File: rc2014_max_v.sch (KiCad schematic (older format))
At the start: 12 parts, among them IC1 SN74ALVC164245DGG, IC2 5M570ZT100I5N, IC3 SN74ALVC164245DGG, J1 Z80 Bus, J2 Pro Bus, J4 M3 Mounting Hole, U1 MIC5356-SGYMME, U2 SN74AVC8T245PW

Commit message: reorganized pins
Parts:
- removed IC1, IC3: SN74ALVC164245DGG, Package_SO:TSSOP-48_6.1x12.5mm_P0.5mm, symbol SN74ALVC164245DGG:SN74ALVC164245DGG
- removed IC2: 5M570ZT100I5N, QFP50P1600X1600X120-100N, symbol 5M570ZT100I5N:5M570ZT100I5N
- removed U2: SN74AVC8T245PW, Package_SO:TSSOP-24_4.4x7.8mm_P0.65mm, symbol Logic_LevelTranslator:SN74AVC8T245PW
- added C10, C11, C12, C13, C14, C15, C16, C5, C6, C7, C8, C9: 100nF, Capacitor_SMD:C_0805_2012Metric_Pad1.15x1.40mm_HandSolder, symbol Device:C
- added U2, U3, U5: SN74ALVC164245DGG, Package_SO:TSSOP-48_6.1x12.5mm_P0.5mm, symbol rc2014_max_v-rescue:SN74ALVC164245DGG
- added U4: 5M570ZT100I5N, Package_QFP:TQFP-100_14x14mm_P0.5mm, symbol rc2014_max_v-rescue:5M570ZT100I5N
- C1, C2, C3, C4: footprint Capacitor_THT:C_Disc_D3.8mm_W2.6mm_P2.50mm -> Capacitor_SMD:C_0805_2012Metric_Pad1.15x1.40mm_HandSolder
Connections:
- net labels added: ~DIR
- wire segments 46 -> 121
- no-connect marks 13 -> 8
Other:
- moved on the sheet: J4

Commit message: numerous changes
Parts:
- removed C13, C15: 100nF, Capacitor_SMD:C_0805_2012Metric_Pad1.15x1.40mm_HandSolder, symbol Device:C
- removed U2, U3, U5: SN74ALVC164245DGG, Package_SO:TSSOP-48_6.1x12.5mm_P0.5mm, symbol rc2014_max_v-rescue:SN74ALVC164245DGG
- C1, C10, C11, C12, C14, C16, C2, C3, C4, C5, C6, C7, C8, C9: footprint Capacitor_SMD:C_0805_2012Metric_Pad1.15x1.40mm_HandSolder -> Capacitor_SMD:C_0603_1608Metric_Pad1.05x0.95mm_HandSolder
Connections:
- net labels removed: DIR, ~DIR
- wire segments 121 -> 74
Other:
- moved on the sheet: C2, C3, C4, U4

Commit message: added FT JTAG
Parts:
- removed U4: 5M570ZT100I5N, Package_QFP:TQFP-100_14x14mm_P0.5mm, symbol rc2014_max_v-rescue:5M570ZT100I5N
- added C13, C15: 100nF, Capacitor_SMD:C_0603_1608Metric_Pad1.05x0.95mm_HandSolder, symbol Device:C
- added J8: Pro Bus, Connector_PinHeader_2.54mm:PinHeader_1x16_P2.54mm_Horizontal, symbol Connector_Generic:Conn_01x16
- added U10, U2, U3, U4: SN74ALVC164245DGG, Package_SO:TSSOP-48_6.1x12.5mm_P0.5mm, symbol rc2014_max_v-rescue:SN74ALVC164245DGG
- J1: value Z80 Bus -> Conn_01x39; footprint Connector_PinHeader_2.54mm:PinHeader_1x39_P2.54mm_Vertical -> Connector_PinHeader_2.54mm:PinHeader_1x39_P2.54mm_Horizontal; MFR - -> (none); MPN - -> (none); SPN - -> (none); SPR - -> (none); SPURL - -> (none)
- J2: value Pro Bus -> Conn_01x10
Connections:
- net labels added: A0_F, A10_F, A11_F, A12_F, A13_F, A14_F, A15_F, A1_F, A2_F, A3_F, A4_F, A5_F, A6_F, A7_F, A8_F, A9_F, CLK_F, D0_F, D1_F, D2_F, D3_F, D4_F, D5_F, D6_F, D7_F, DIR, GPIO_1, GPIO_10, GPIO_11, GPIO_12, GPIO_13, GPIO_14, GPIO_15, GPIO_16, GPIO_2, GPIO_3, GPIO_4, GPIO_5, GPIO_6, GPIO_7, GPIO_8, GPIO_9, OE_A, OE_C_I, OE_C_O, OE_D, RX_A, TX_A, ~BUSACK_F, ~DIR, ~IORQ_F, ~M1_F, ~MREQ_F, ~PAGE_F, ~RD_F, ~WR_F
- wire segments 74 -> 114
- no-connect marks 8 -> 5
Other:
- moved on the sheet: C1, C2, C3, C4, J4

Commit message: replaced single resistors with arrays
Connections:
- net labels added: RX_A_F, ~BUSRQ_F, ~HALT_F, ~INT_F, ~NMI_F, ~RESET2_F, ~RESET_F, ~WAIT_F
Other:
- moved on the sheet: C10, C11, C12, C13, C14, C15, C16, C2, C3, C4, C5, C6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

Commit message: fixed up GPIO, started layout
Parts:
- removed U10: SN74ALVC164245DGG, Package_SO:TSSOP-48_6.1x12.5mm_P0.5mm, symbol rc2014_max_v-rescue:SN74ALVC164245DGG
- added C16, C17: 100nF, Capacitor_SMD:C_0603_1608Metric_Pad1.05x0.95mm_HandSolder, symbol Device:C
- added R1, R2: 50K, Resistor_SMD:R_0603_1608Metric_Pad1.05x0.95mm_HandSolder, symbol Device:R_Small
- added U4, U5: TXB0108PWR, Package_SO:TSSOP-20_4.4x6.5mm_P0.65mm, symbol Logic_LevelTranslator:TXB0108PWR
- J2: renamed from J1; value Conn_01x39 -> Conn_01x40; footprint Connector_PinHeader_2.54mm:PinHeader_1x39_P2.54mm_Horizontal -> Connector_PinHeader_2.54mm:PinHeader_1x40_P2.54mm_Horizontal; symbol Connector_Generic:Conn_01x39 -> Connector_Generic:Conn_01x40
- J4: renamed from J2; value Conn_01x10 -> Conn_01x24; footprint Connector_PinHeader_2.54mm:PinHeader_1x10_P2.54mm_Vertical -> Connector_PinHeader_2.54mm:PinHeader_1x24_P2.54mm_Vertical; symbol Connector_Generic:Conn_01x10 -> Connector_Generic:Conn_01x24
- U1: symbol Regulator_Linear:MIC5356-SGYMME -> rc2014_max_v-rescue:MIC5356-SGYMME-Regulator_Linear
- renumbered C11 to C1, C5 to C10, C6 to C11, C7 to C12, C8 to C13, C9 to C14, C10 to C15, C1 to C18, C12 to C2, C13 to C3, C14 to C4, C15 to C5, C16 to C6, C3 to C7, C2 to C8, C4 to C9, J4 to J1, J8 to J3, U4 to U2, U2 to U6
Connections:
- net labels added: D10, D10_F, D11, D11_F, D12, D12_F, D13, D13_F, D14, D14_F, D15, D15_F, D8, D8_F, D9, D9_F, OE_G_1, OE_G_2, RX_B, TX_B
- wire segments 114 -> 113
- no-connect marks 5 -> 9
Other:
- moved on the sheet: C1, C10, C11, C12, C13, C14, C15, C2, C3, C4, C5, C6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

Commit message: Added logo, cpio vcc selection
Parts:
- added JP1: Jumper_3_Bridged12, Connector_PinHeader_2.54mm:PinHeader_1x03_P2.54mm_Vertical, symbol Jumper:Jumper_3_Bridged12
- U4, U5: symbol Logic_LevelTranslator:TXB0108PWR -> rc2014_max_v-rescue:TXB0108PWR-Logic_LevelTranslator
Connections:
- net +3V3: now also JP1.1 (A)
- net +5V: now also JP1.3 (B); no longer C16.1, C17.1, U4.19 (VCCB), U5.19 (VCCB)
- new net VCC_GPIO: C16.1, C17.1, JP1.2 (C), U4.19 (VCCB), U5.19 (VCCB)
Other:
- moved on the sheet: C16, C17, R2, U5

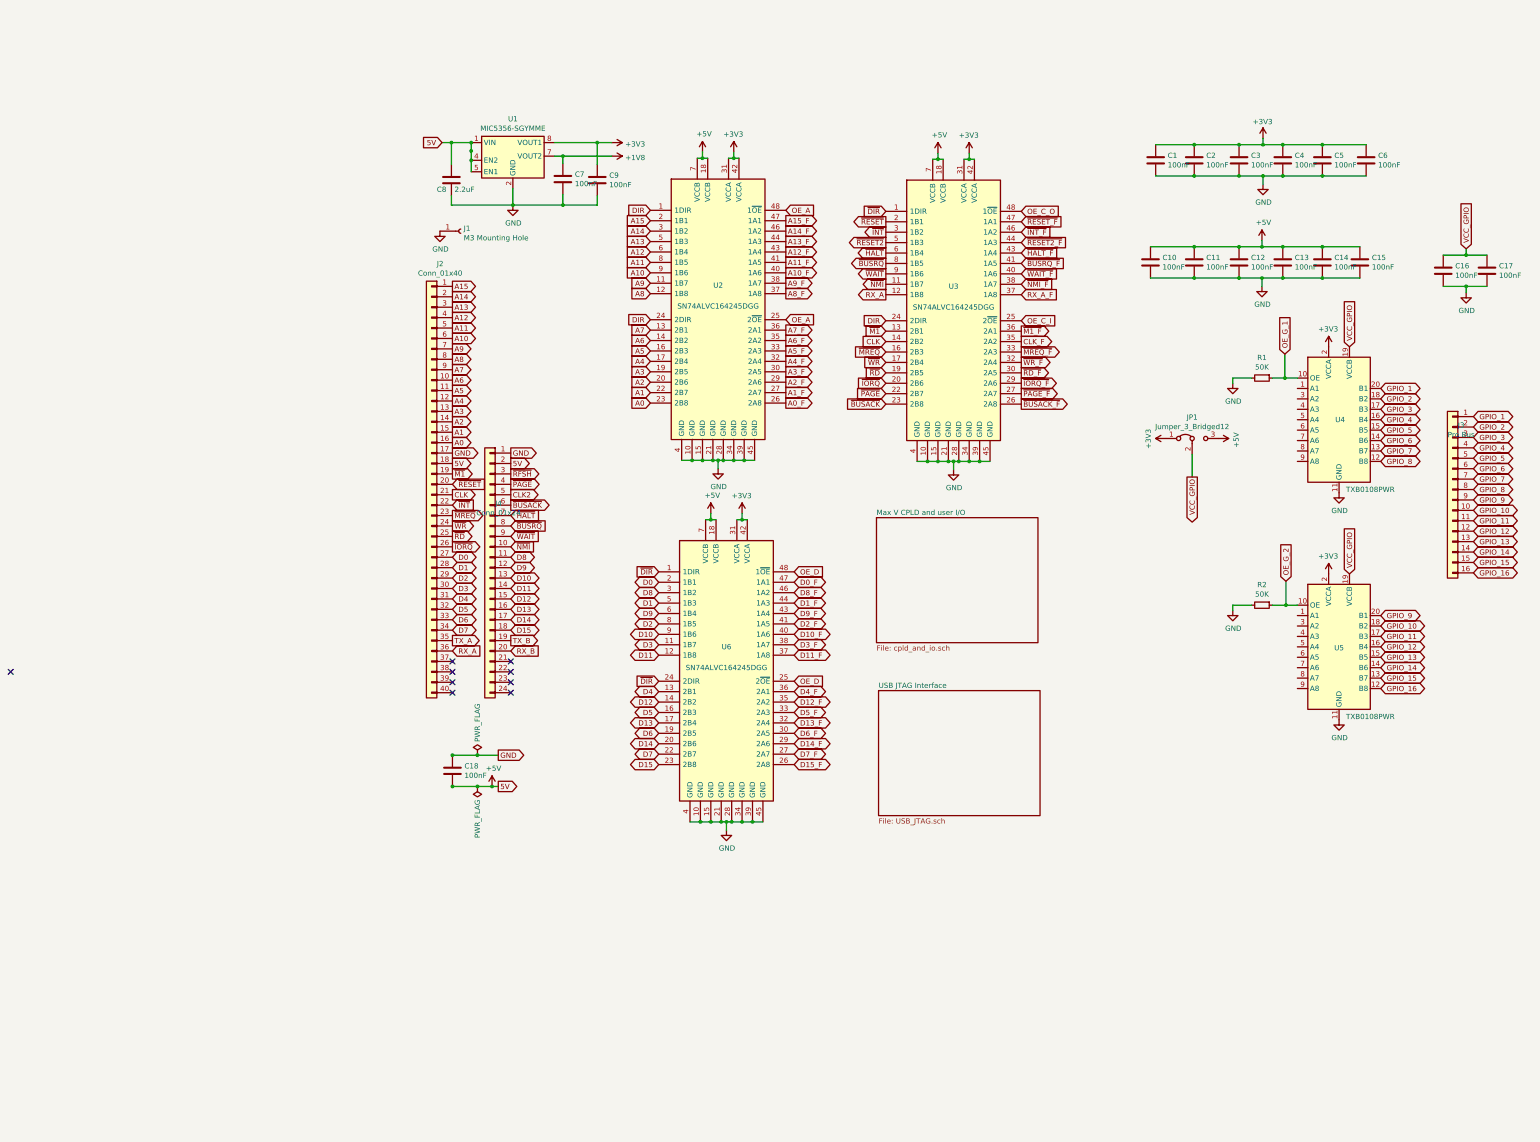
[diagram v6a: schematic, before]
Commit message: larger maxv, additional clocks, reorganized sheets
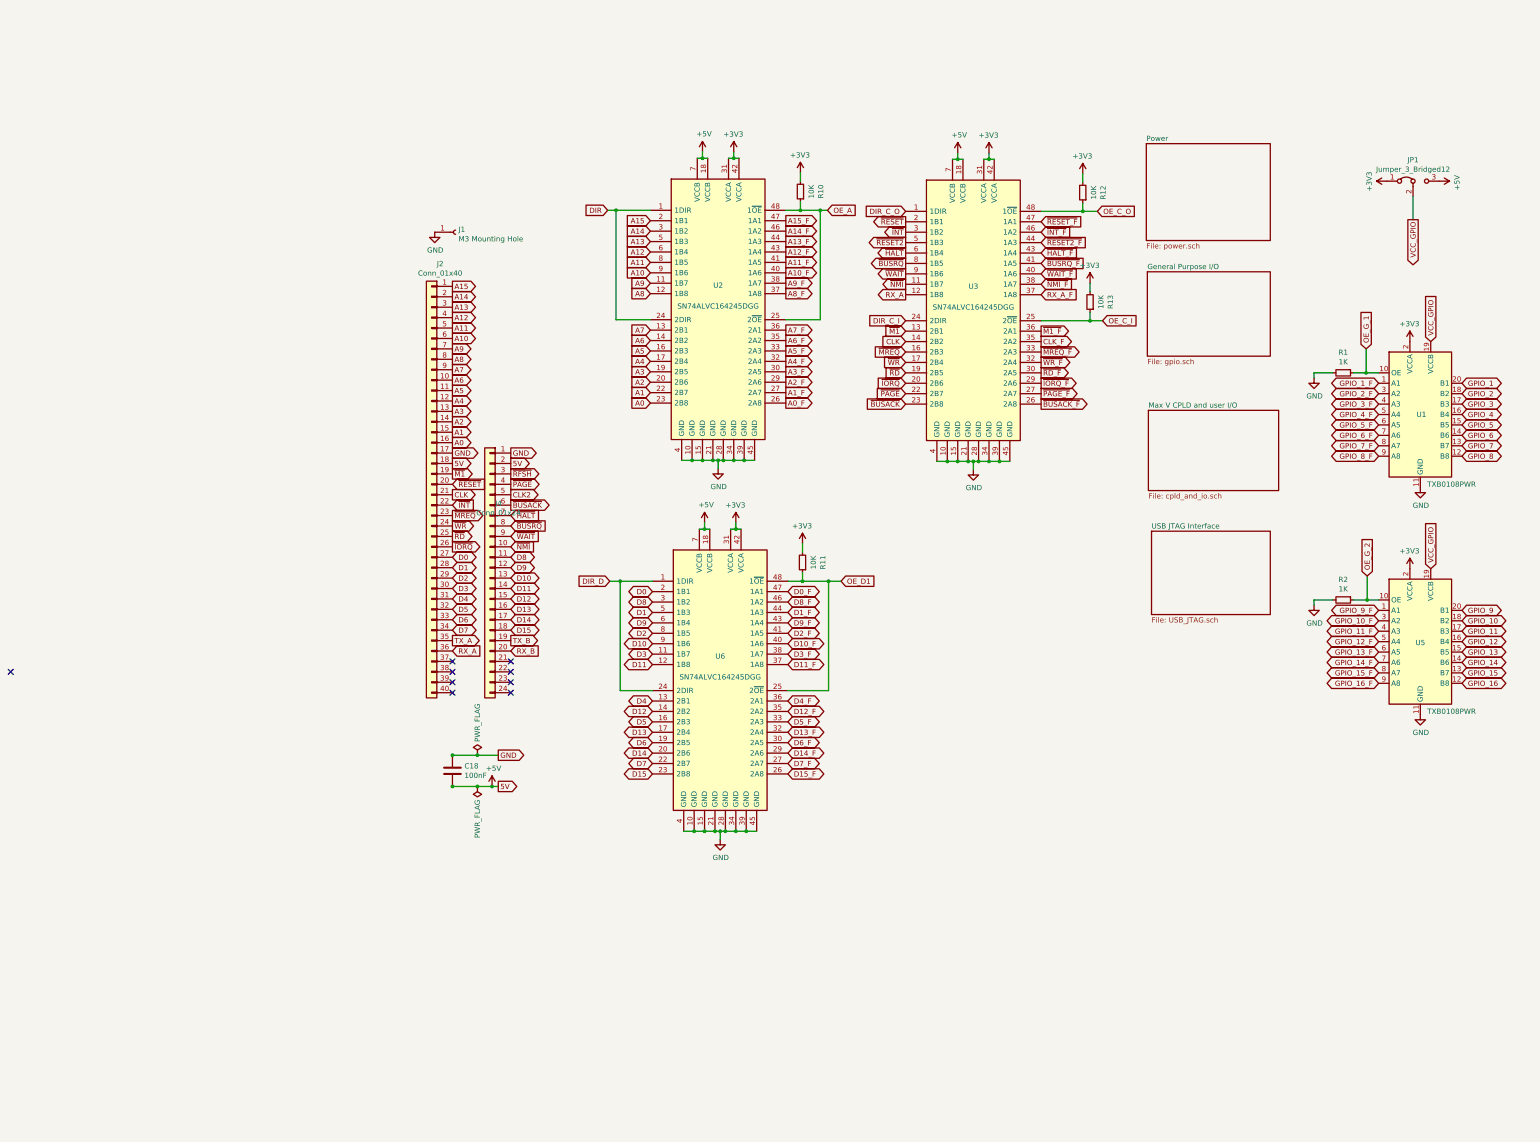
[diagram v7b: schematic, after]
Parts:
- removed C1, C10, C11, C12, C13, C14, C15, C16, C17, C2, C3, C4, C5, C6, C7, C9: 100nF, Capacitor_SMD:C_0603_1608Metric_Pad1.05x0.95mm_HandSolder, symbol Device:C
- removed C8: 2.2uF, Capacitor_SMD:C_0603_1608Metric_Pad1.05x0.95mm_HandSolder, symbol Device:C
- removed J3: Pro Bus, Connector_PinHeader_2.54mm:PinHeader_1x16_P2.54mm_Horizontal, symbol Connector_Generic:Conn_01x16
- removed U1: MIC5356-SGYMME, Package_SO:MSOP-8-1EP_3x3mm_P0.65mm_EP2.5x3mm_Mask1.73x2.36mm_ThermalVias, symbol rc2014_max_v-rescue:MIC5356-SGYMME-Regulator_Linear
- removed U4: TXB0108PWR, Package_SO:TSSOP-20_4.4x6.5mm_P0.65mm, symbol rc2014_max_v-rescue:TXB0108PWR-Logic_LevelTranslator
- added R10, R11, R12, R13: 10K, Resistor_SMD:R_0603_1608Metric_Pad1.05x0.95mm_HandSolder, symbol Device:R_Small
- added U1: TXB0108PWR, Package_SO:TSSOP-20_4.4x6.5mm_P0.65mm, symbol rc2014_max_v-rescue:TXB0108PWR-Logic_LevelTranslator
- R1, R2: value 50K -> 1K
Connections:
- net +3V3: now also R10.2, R11.2, R12.2, R13.2, U1.2 (VCCA)
- net DIR: no longer U3.24 (2DIR)
- net GND: now also U1.11 (GND)
- net GPIO_1: now also U1.20 (B1)
- net GPIO_2: now also U1.18 (B2)
- net GPIO_3: now also U1.17 (B3)
- net GPIO_4: now also U1.16 (B4)
- net GPIO_5: now also U1.15 (B5)
- net GPIO_6: now also U1.14 (B6)
- net GPIO_7: now also U1.13 (B7)
- net GPIO_8: now also U1.12 (B8)
- net OE_A: now also R10.1
- net OE_C_I: now also R13.1
- net OE_C_O: now also R12.1
- net OE_G_1: now also U1.10 (OE)
- net VCC_GPIO: now also U1.19 (VCCB)
- net GPIO_9_F: now reaches U5.1 (A1)
- net GPIO_10_F: now reaches U5.3 (A2)
- net GPIO_11_F: now reaches U5.4 (A3)
- net GPIO_12_F: now reaches U5.5 (A4)
- net GPIO_13_F: now reaches U5.6 (A5)
- net GPIO_14_F: now reaches U5.7 (A6)
- net GPIO_15_F: now reaches U5.8 (A7)
- net GPIO_16_F: now reaches U5.9 (A8)
- net OE_D renamed OE_D1
- net OE_D1: now also R11.1
- net ~DIR renamed DIR_D
- net DIR_D: no longer U3.1 (1DIR)
- new net DIR_C_I: U3.24 (2DIR)
- new net DIR_C_O: U3.1 (1DIR)
- new net GPIO_1_F: U1.1 (A1)
- new net GPIO_2_F: U1.3 (A2)
- new net GPIO_3_F: U1.4 (A3)
- new net GPIO_4_F: U1.5 (A4)
- new net GPIO_5_F: U1.6 (A5)
- new net GPIO_6_F: U1.7 (A6)
- new net GPIO_7_F: U1.8 (A7)
- new net GPIO_8_F: U1.9 (A8)
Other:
- moved on the sheet: J1, U3, U6

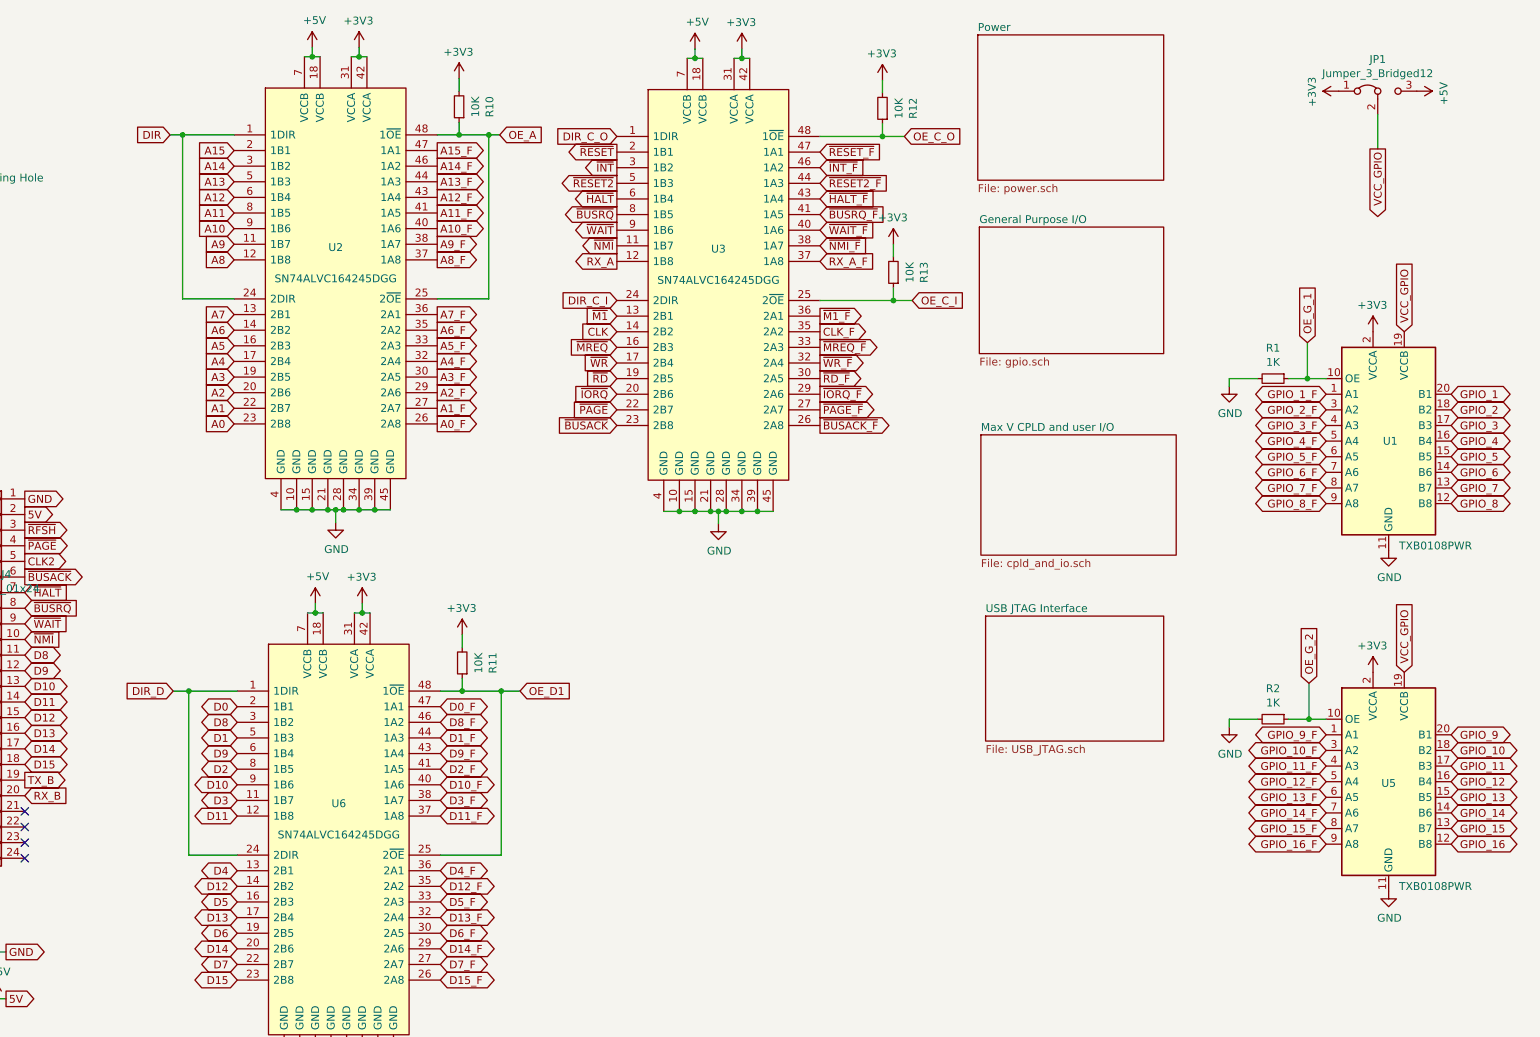
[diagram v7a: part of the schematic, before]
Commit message: organized bypass caps
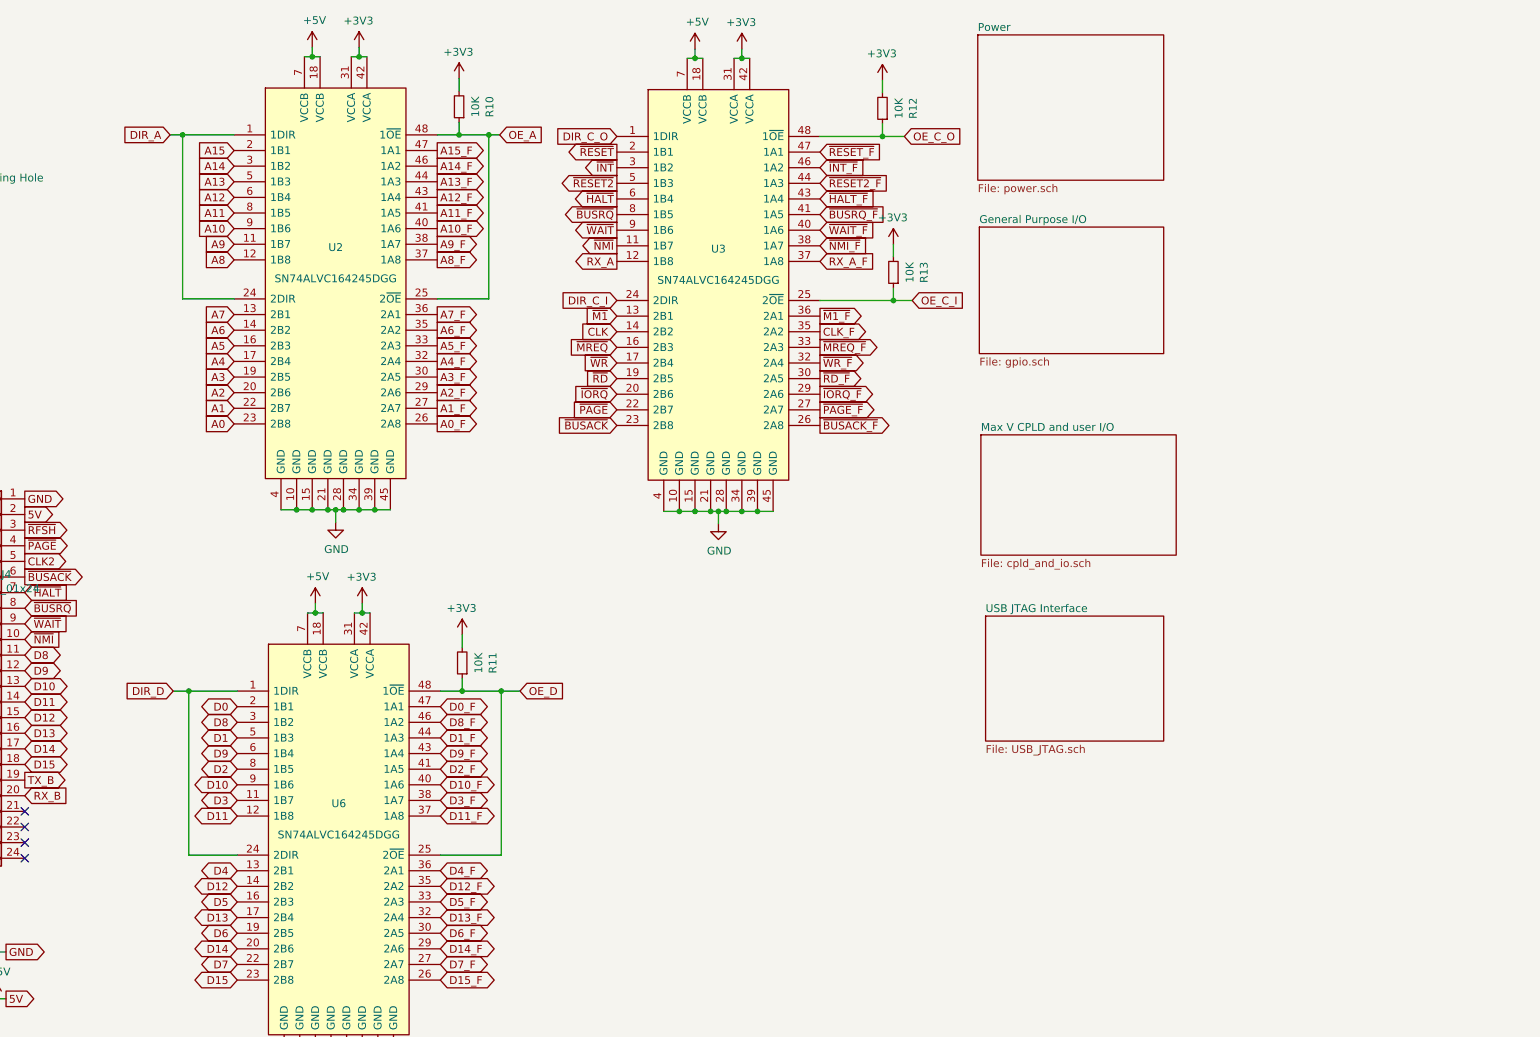
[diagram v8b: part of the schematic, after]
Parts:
- removed JP1: Jumper_3_Bridged12, Connector_PinHeader_2.54mm:PinHeader_1x03_P2.54mm_Vertical, symbol Jumper:Jumper_3_Bridged12
- removed R1, R2: 1K, Resistor_SMD:R_0603_1608Metric_Pad1.05x0.95mm_HandSolder, symbol Device:R_Small
- removed U1, U5: TXB0108PWR, Package_SO:TSSOP-20_4.4x6.5mm_P0.65mm, symbol rc2014_max_v-rescue:TXB0108PWR-Logic_LevelTranslator
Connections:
- net DIR renamed DIR_A
- net OE_D1 renamed OE_D
